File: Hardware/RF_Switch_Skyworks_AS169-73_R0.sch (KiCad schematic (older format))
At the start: 5 parts, among them U4 AS169-73

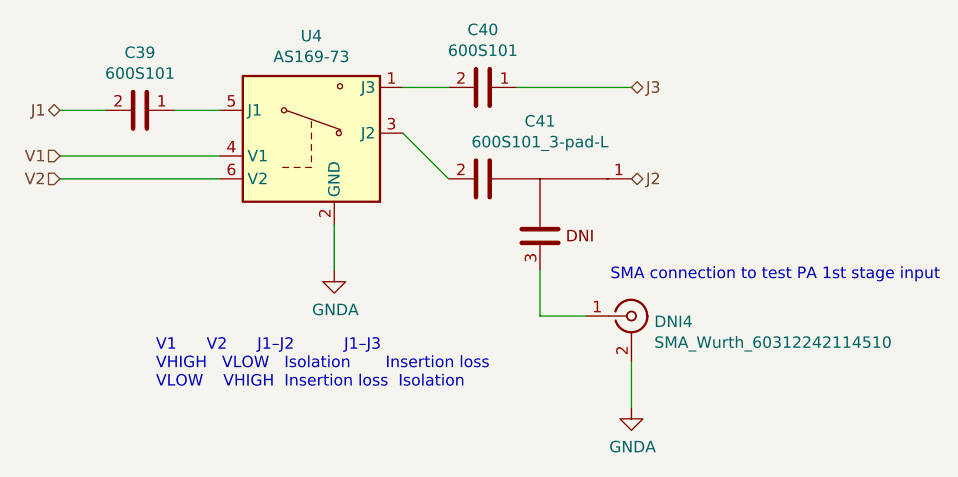
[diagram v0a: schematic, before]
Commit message: Added discrete Chebyshev input filter to schematic based on Qucs simulationd. Artwork not done. It has occurred to me that I need to do some major cleanup of the test points on this PCBA.
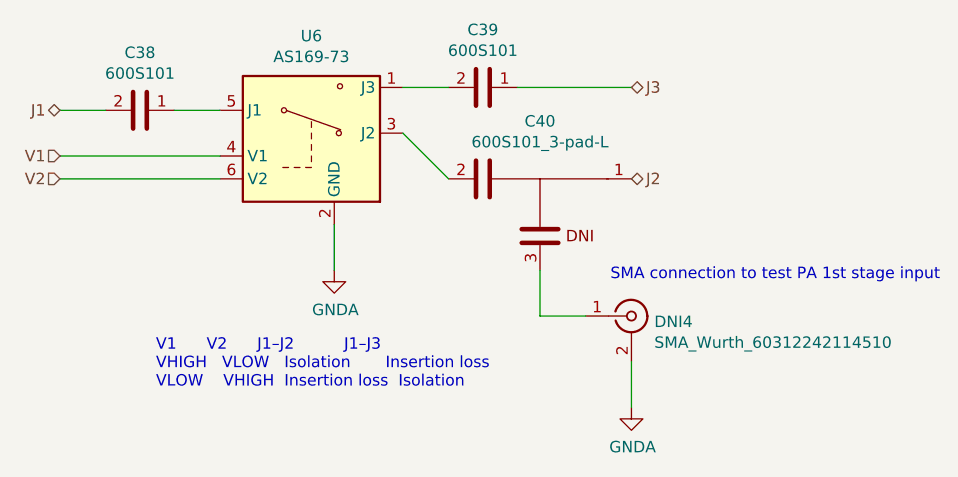
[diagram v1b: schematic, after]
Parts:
- renumbered C30 to C29, C31 to C30, C41 to C40
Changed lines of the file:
@@
 $Descr A4 11693 8268
 encoding utf-8
-Sheet 11 12
+Sheet 11 16
 Title ""
 Date ""
@@
 AR Path="/5F11BFA6/5F30E7DD" Ref="#PWR?"  Part="1"
 AR Path="/5F11C68E/5F30E7DD" Ref="#PWR?"  Part="1"
-AR Path="/5F20A94F/5F30E7DD" Ref="#PWR040"  Part="1"
+AR Path="/5F20A94F/5F30E7DD" Ref="#PWR037"  Part="1"
 AR Path="/5F20D989/5F30E7DD" Ref="#PWR?"  Part="1"
-AR Path="/5F20DB0B/5F30E7DD" Ref="#PWR049"  Part="1"
+AR Path="/5F20DB0B/5F30E7DD" Ref="#PWR046"  Part="1"
 AR Path="/5F2751D2/5F30E7DD" Ref="#PWR?"  Part="1"
-F 0 "#PWR049" H 5600 3850 50  0001 C CNN
+F 0 "#PWR046" H 5600 3850 50  0001 C CNN
 F 1 "GNDA" H 5605 3927 50  0000 C CNN
 F 2 "" H 5600 4100 50  0001 C CNN
@@
 AR Path="/5F11BFA6/5F30E7DE" Ref="C?"  Part="1"
 AR Path="/5F11C68E/5F30E7DE" Ref="C?"  Part="1"
-AR Path="/5F20A94F/5F30E7DE" Ref="C30"  Part="1"
+AR Path="/5F20A94F/5F30E7DE" Ref="C29"  Part="1"
 AR Path="/5F20D989/5F30E7DE" Ref="C?"  Part="1"
-AR Path="/5F20DB0B/5F30E7DE" Ref="C39"  Part="1"
+AR Path="/5F20DB0B/5F30E7DE" Ref="C38"  Part="1"
 AR Path="/5F2751D2/5F30E7DE" Ref="C?"  Part="1"
-F 0 "C39" V 4498 3400 50  0000 C CNN
+F 0 "C38" V 4498 3400 50  0000 C CNN
 F 1 "600S101" V 4589 3400 50  0000 C CNN
 F 2 "Capacitor_SMD:C_0603_1608Metric" H 4800 3500 50  0001 C CNN
@@
 AR Path="/5F11BFA6/5F11A939" Ref="C?"  Part="1"
 AR Path="/5F11C68E/5F11A939" Ref="C?"  Part="1"
-AR Path="/5F20A94F/5F11A939" Ref="C31"  Part="1"
+AR Path="/5F20A94F/5F11A939" Ref="C30"  Part="1"
 AR Path="/5F20D989/5F11A939" Ref="C?"  Part="1"
-AR Path="/5F20DB0B/5F11A939" Ref="C40"  Part="1"
+AR Path="/5F20DB0B/5F11A939" Ref="C39"  Part="1"
 AR Path="/5F2751D2/5F11A939" Ref="C?"  Part="1"
-F 0 "C40" V 5998 3300 50  0000 C CNN
+F 0 "C39" V 5998 3300 50  0000 C CNN
 F 1 "600S101" V 6089 3300 50  0000 C CNN
 F 2 "Capacitor_SMD:C_0603_1608Metric" H 6300 3400 50  0001 C CNN
@@
 AR Path="/5F11BFA6/5F303E0E" Ref="#PWR?"  Part="1"
 AR Path="/5F11C68E/5F303E0E" Ref="#PWR?"  Part="1"
-AR Path="/5F20A94F/5F303E0E" Ref="#PWR041"  Part="1"
+AR Path="/5F20A94F/5F303E0E" Ref="#PWR038"  Part="1"
 AR Path="/5F20D989/5F303E0E" Ref="#PWR?"  Part="1"
-AR Path="/5F20DB0B/5F303E0E" Ref="#PWR050"  Part="1"
+AR Path="/5F20DB0B/5F303E0E" Ref="#PWR047"  Part="1"
 AR Path="/5F2751D2/5F303E0E" Ref="#PWR?"  Part="1"
-F 0 "#PWR050" H 6900 4450 50  0001 C CNN
+F 0 "#PWR047" H 6900 4450 50  0001 C CNN
 F 1 "GNDA" H 6905 4527 50  0000 C CNN
 F 2 "" H 6900 4700 50  0001 C CNN
@@
 J2
 $Comp
-L ATC:600S101_3-pad-L C41
+L ATC:600S101_3-pad-L C40
 U 1 1 5F339855
 P 6500 3700
-AR Path="/5F20DB0B/5F339855" Ref="C41"  Part="1"
-AR Path="/5F20A94F/5F339855" Ref="C32"  Part="1"
-F 0 "C41" H 6500 3448 50  0000 C CNN
+AR Path="/5F20DB0B/5F339855" Ref="C40"  Part="1"
+AR Path="/5F20A94F/5F339855" Ref="C31"  Part="1"
+F 0 "C40" H 6500 3448 50  0000 C CNN
 F 1 "600S101_3-pad-L" H 6500 3539 50  0000 C CNN
 F 2 "Capacitor_SMD:C_0603_1608Metric_3-pad-L" H 7400 2950 50  0001 C CNN
@@
 AR Path="/5F20DB0B/5F303E09" Ref="U6"  Part="1"
 AR Path="/5F2751D2/5F303E09" Ref="U?"  Part="1"
-F 0 "U4" H 5500 3925 50  0000 C CNN
+F 0 "U6" H 5500 3925 50  0000 C CNN
 F 1 "AS169-73" H 5500 3834 50  0000 C CNN
 F 2 "Package_TO_SOT_SMD:SOT-23-6" H 5600 3500 50  0001 C CNN

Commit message: Major cleanup to both the schematic and directory structure. Stackup has changed accomodate to 0.65mm trace width. Chebyshev filter lived through the experience in the Qucs simulation; others not checked yet. I do want to re-visit the matching networks of all of the amplifiers as I have developed some good strategies to implement them.
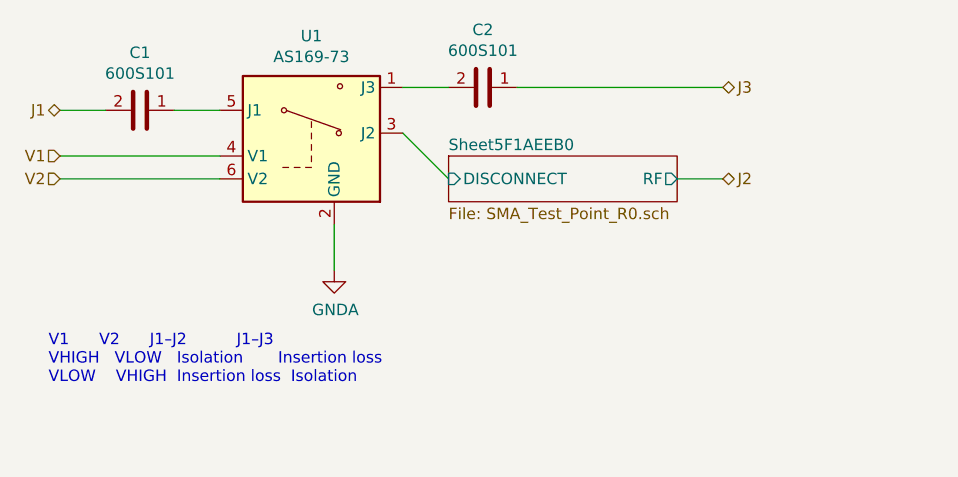
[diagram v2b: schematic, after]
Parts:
- removed C40: 600S101_3-pad-L, Capacitor_SMD:C_0603_1608Metric_3-pad-L, symbol ATC:600S101_3-pad-L
- removed DNI4: SMA_Wurth_60312242114510, RF:SMA_Wurth_60312242114510, symbol RF:SMA_Wurth_60312242114510
- renumbered C29 to C1, C30 to C2, U4 to U1
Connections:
- net Sheet5F1AEEB0/DISCONNECT: now reaches U1.3 (J2)
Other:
- note removed: "SMA connection to test PA 1st stage input"
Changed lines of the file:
@@
 $Descr A4 11693 8268
 encoding utf-8
-Sheet 11 16
+Sheet 3 24
 Title ""
 Date ""
@@
 AR Path="/5F11BFA6/5F30E7DD" Ref="#PWR?"  Part="1"
 AR Path="/5F11C68E/5F30E7DD" Ref="#PWR?"  Part="1"
-AR Path="/5F20A94F/5F30E7DD" Ref="#PWR037"  Part="1"
+AR Path="/5F20A94F/5F30E7DD" Ref="#PWR06"  Part="1"
 AR Path="/5F20D989/5F30E7DD" Ref="#PWR?"  Part="1"
-AR Path="/5F20DB0B/5F30E7DD" Ref="#PWR046"  Part="1"
+AR Path="/5F20DB0B/5F30E7DD" Ref="#PWR015"  Part="1"
 AR Path="/5F2751D2/5F30E7DD" Ref="#PWR?"  Part="1"
-F 0 "#PWR046" H 5600 3850 50  0001 C CNN
+F 0 "#PWR06" H 5600 3850 50  0001 C CNN
 F 1 "GNDA" H 5605 3927 50  0000 C CNN
 F 2 "" H 5600 4100 50  0001 C CNN
@@
 	1    0    0    -1
 $EndComp
-Text Notes 4820 4620 0    50   ~ 0
-V1      V2      J1–J2          J1–J3\nVHIGH   VLOW   Isolation       Insertion loss\nVLOW    VHIGH  Insertion loss  Isolation
 Wire Wire Line
 	4900 3400 5100 3400
@@
 Text HLabel 4400 3400 0    50   BiDi ~ 0
 J1
-Text HLabel 6900 3300 2    50   BiDi ~ 0
+Text HLabel 7300 3300 2    50   BiDi ~ 0
 J3
 Text HLabel 4400 3600 0    50   Input ~ 0
@@
 AR Path="/5F11BFA6/5F30E7DE" Ref="C?"  Part="1"
 AR Path="/5F11C68E/5F30E7DE" Ref="C?"  Part="1"
-AR Path="/5F20A94F/5F30E7DE" Ref="C29"  Part="1"
+AR Path="/5F20A94F/5F30E7DE" Ref="C1"  Part="1"
 AR Path="/5F20D989/5F30E7DE" Ref="C?"  Part="1"
-AR Path="/5F20DB0B/5F30E7DE" Ref="C38"  Part="1"
+AR Path="/5F20DB0B/5F30E7DE" Ref="C10"  Part="1"
 AR Path="/5F2751D2/5F30E7DE" Ref="C?"  Part="1"
-F 0 "C38" V 4498 3400 50  0000 C CNN
+F 0 "C1" V 4498 3400 50  0000 C CNN
 F 1 "600S101" V 4589 3400 50  0000 C CNN
 F 2 "Capacitor_SMD:C_0603_1608Metric" H 4800 3500 50  0001 C CNN
@@
 AR Path="/5F11BFA6/5F11A939" Ref="C?"  Part="1"
 AR Path="/5F11C68E/5F11A939" Ref="C?"  Part="1"
-AR Path="/5F20A94F/5F11A939" Ref="C30"  Part="1"
+AR Path="/5F20A94F/5F11A939" Ref="C2"  Part="1"
 AR Path="/5F20D989/5F11A939" Ref="C?"  Part="1"
-AR Path="/5F20DB0B/5F11A939" Ref="C39"  Part="1"
+AR Path="/5F20DB0B/5F11A939" Ref="C11"  Part="1"
 AR Path="/5F2751D2/5F11A939" Ref="C?"  Part="1"
-F 0 "C39" V 5998 3300 50  0000 C CNN
+F 0 "C2" V 5998 3300 50  0000 C CNN
 F 1 "600S101" V 6089 3300 50  0000 C CNN
 F 2 "Capacitor_SMD:C_0603_1608Metric" H 6300 3400 50  0001 C CNN
@@
 $EndComp
 Wire Wire Line
-	6400 3300 6900 3300
-$Comp
-L RF:SMA_Wurth_60312242114510 DNI4
-U 1 1 5F303E0D
-P 6900 4300
-AR Path="/5F20DB0B/5F303E0D" Ref="DNI4"  Part="1"
-AR Path="/5F20A94F/5F303E0D" Ref="DNI3"  Part="1"
-AR Path="/5F2751D2/5F303E0D" Ref="DNI?"  Part="1"
-F 0 "DNI4" H 7000 4275 50  0000 L CNN
-F 1 "SMA_Wurth_60312242114510" H 7000 4184 50  0000 L CNN
-F 2 "RF:SMA_Wurth_60312242114510" H 6900 4300 50  0001 C CNN
-F 3 "https://www.we-online.de/katalog/datasheet/60312242114510.pdf" H 6900 4300 50  0001 C CNN
-	1    6900 4300
-	1    0    0    -1
-$EndComp
-Wire Wire Line
-	6500 4300 6700 4300
-$Comp
-L power:GNDA #PWR?
-U 1 1 5F303E0E
-P 6900 4700
-AR Path="/5F1FE880/5F303E0E" Ref="#PWR?"  Part="1"
-AR Path="/5F19C733/5F303E0E" Ref="#PWR?"  Part="1"
-AR Path="/5F19DDB3/5F303E0E" Ref="#PWR?"  Part="1"
-AR Path="/5F11BFA6/5F303E0E" Ref="#PWR?"  Part="1"
-AR Path="/5F11C68E/5F303E0E" Ref="#PWR?"  Part="1"
-AR Path="/5F20A94F/5F303E0E" Ref="#PWR038"  Part="1"
-AR Path="/5F20D989/5F303E0E" Ref="#PWR?"  Part="1"
-AR Path="/5F20DB0B/5F303E0E" Ref="#PWR047"  Part="1"
-AR Path="/5F2751D2/5F303E0E" Ref="#PWR?"  Part="1"
-F 0 "#PWR047" H 6900 4450 50  0001 C CNN
-F 1 "GNDA" H 6905 4527 50  0000 C CNN
-F 2 "" H 6900 4700 50  0001 C CNN
-F 3 "" H 6900 4700 50  0001 C CNN
-	1    6900 4700
-	1    0    0    -1
-$EndComp
-Wire Wire Line
-	6900 4500 6900 4700
-Text Notes 8250 4150 2    50   ~ 0
-SMA connection to test PA 1st stage input
-Wire Wire Line
-	6500 4100 6500 4300
-Wire Wire Line
 	5900 3500 6100 3700
-Text HLabel 6900 3700 2    50   BiDi ~ 0
+Text HLabel 7300 3700 2    50   BiDi ~ 0
 J2
-$Comp
-L ATC:600S101_3-pad-L C40
-U 1 1 5F339855
-P 6500 3700
-AR Path="/5F20DB0B/5F339855" Ref="C40"  Part="1"
-AR Path="/5F20A94F/5F339855" Ref="C31"  Part="1"
-F 0 "C40" H 6500 3448 50  0000 C CNN
-F 1 "600S101_3-pad-L" H 6500 3539 50  0000 C CNN
-F 2 "Capacitor_SMD:C_0603_1608Metric_3-pad-L" H 7400 2950 50  0001 C CNN
-F 3 "" V 6500 3650 50  0001 C CNN
-	1    6500 3700
-	1    0    0    1
-$EndComp
 $Comp
 L RF_Switch:AS169-73 U?
@@
 AR Path="/5F11BFA6/5F303E09" Ref="U?"  Part="1"
 AR Path="/5F11C68E/5F303E09" Ref="U?"  Part="1"
-AR Path="/5F20A94F/5F303E09" Ref="U4"  Part="1"
+AR Path="/5F20A94F/5F303E09" Ref="U1"  Part="1"
 AR Path="/5F20D989/5F303E09" Ref="U?"  Part="1"
-AR Path="/5F20DB0B/5F303E09" Ref="U6"  Part="1"
+AR Path="/5F20DB0B/5F303E09" Ref="U3"  Part="1"
 AR Path="/5F2751D2/5F303E09" Ref="U?"  Part="1"
-F 0 "U6" H 5500 3925 50  0000 C CNN
+F 0 "U1" H 5500 3925 50  0000 C CNN
 F 1 "AS169-73" H 5500 3834 50  0000 C CNN
 F 2 "Package_TO_SOT_SMD:SOT-23-6" H 5600 3500 50  0001 C CNN
@@
 	1    0    0    -1
 $EndComp
+$Sheet
+S 6100 3600 1000 200
+U 5F1AEEB1
+F0 "Sheet5F1AEEB0" 50
+F1 "SMA_Test_Point_R0.sch" 50
+F2 "DISCONNECT" I L 6100 3700 50
+F3 "RF" O R 7100 3700 50
+$EndSheet
+Text Notes 4350 4600 0    50   ~ 0
+V1      V2      J1–J2          J1–J3\nVHIGH   VLOW   Isolation       Insertion loss\nVLOW    VHIGH  Insertion loss  Isolation
+Wire Wire Line
+	6400 3300 7300 3300
+Wire Wire Line
+	7100 3700 7300 3700
 $EndSCHEMATC

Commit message: Improving LNA simulations and Documentation package. More to come on this one.
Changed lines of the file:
@@
 $Descr A4 11693 8268
 encoding utf-8
-Sheet 3 24
+Sheet 6 23
 Title ""
 Date ""
@@
 AR Path="/5F20A94F/5F30E7DD" Ref="#PWR06"  Part="1"
 AR Path="/5F20D989/5F30E7DD" Ref="#PWR?"  Part="1"
-AR Path="/5F20DB0B/5F30E7DD" Ref="#PWR015"  Part="1"
+AR Path="/5F20DB0B/5F30E7DD" Ref="#PWR017"  Part="1"
 AR Path="/5F2751D2/5F30E7DD" Ref="#PWR?"  Part="1"
-F 0 "#PWR06" H 5600 3850 50  0001 C CNN
+F 0 "#PWR017" H 5600 3850 50  0001 C CNN
 F 1 "GNDA" H 5605 3927 50  0000 C CNN
 F 2 "" H 5600 4100 50  0001 C CNN
@@
 AR Path="/5F20A94F/5F30E7DE" Ref="C1"  Part="1"
 AR Path="/5F20D989/5F30E7DE" Ref="C?"  Part="1"
-AR Path="/5F20DB0B/5F30E7DE" Ref="C10"  Part="1"
+AR Path="/5F20DB0B/5F30E7DE" Ref="C13"  Part="1"
 AR Path="/5F2751D2/5F30E7DE" Ref="C?"  Part="1"
-F 0 "C1" V 4498 3400 50  0000 C CNN
+F 0 "C13" V 4498 3400 50  0000 C CNN
 F 1 "600S101" V 4589 3400 50  0000 C CNN
 F 2 "Capacitor_SMD:C_0603_1608Metric" H 4800 3500 50  0001 C CNN
@@
 AR Path="/5F20A94F/5F11A939" Ref="C2"  Part="1"
 AR Path="/5F20D989/5F11A939" Ref="C?"  Part="1"
-AR Path="/5F20DB0B/5F11A939" Ref="C11"  Part="1"
+AR Path="/5F20DB0B/5F11A939" Ref="C14"  Part="1"
 AR Path="/5F2751D2/5F11A939" Ref="C?"  Part="1"
-F 0 "C2" V 5998 3300 50  0000 C CNN
+F 0 "C14" V 5998 3300 50  0000 C CNN
 F 1 "600S101" V 6089 3300 50  0000 C CNN
 F 2 "Capacitor_SMD:C_0603_1608Metric" H 6300 3400 50  0001 C CNN
@@
 AR Path="/5F20DB0B/5F303E09" Ref="U3"  Part="1"
 AR Path="/5F2751D2/5F303E09" Ref="U?"  Part="1"
-F 0 "U1" H 5500 3925 50  0000 C CNN
+F 0 "U3" H 5500 3925 50  0000 C CNN
 F 1 "AS169-73" H 5500 3834 50  0000 C CNN
 F 2 "Package_TO_SOT_SMD:SOT-23-6" H 5600 3500 50  0001 C CNN
